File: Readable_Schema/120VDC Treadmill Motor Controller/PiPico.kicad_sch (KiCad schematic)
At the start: 5 parts, among them J3 TB0011-350-08BE, J4 TB0011-350-08BE, J5 TB0011-350-08BE

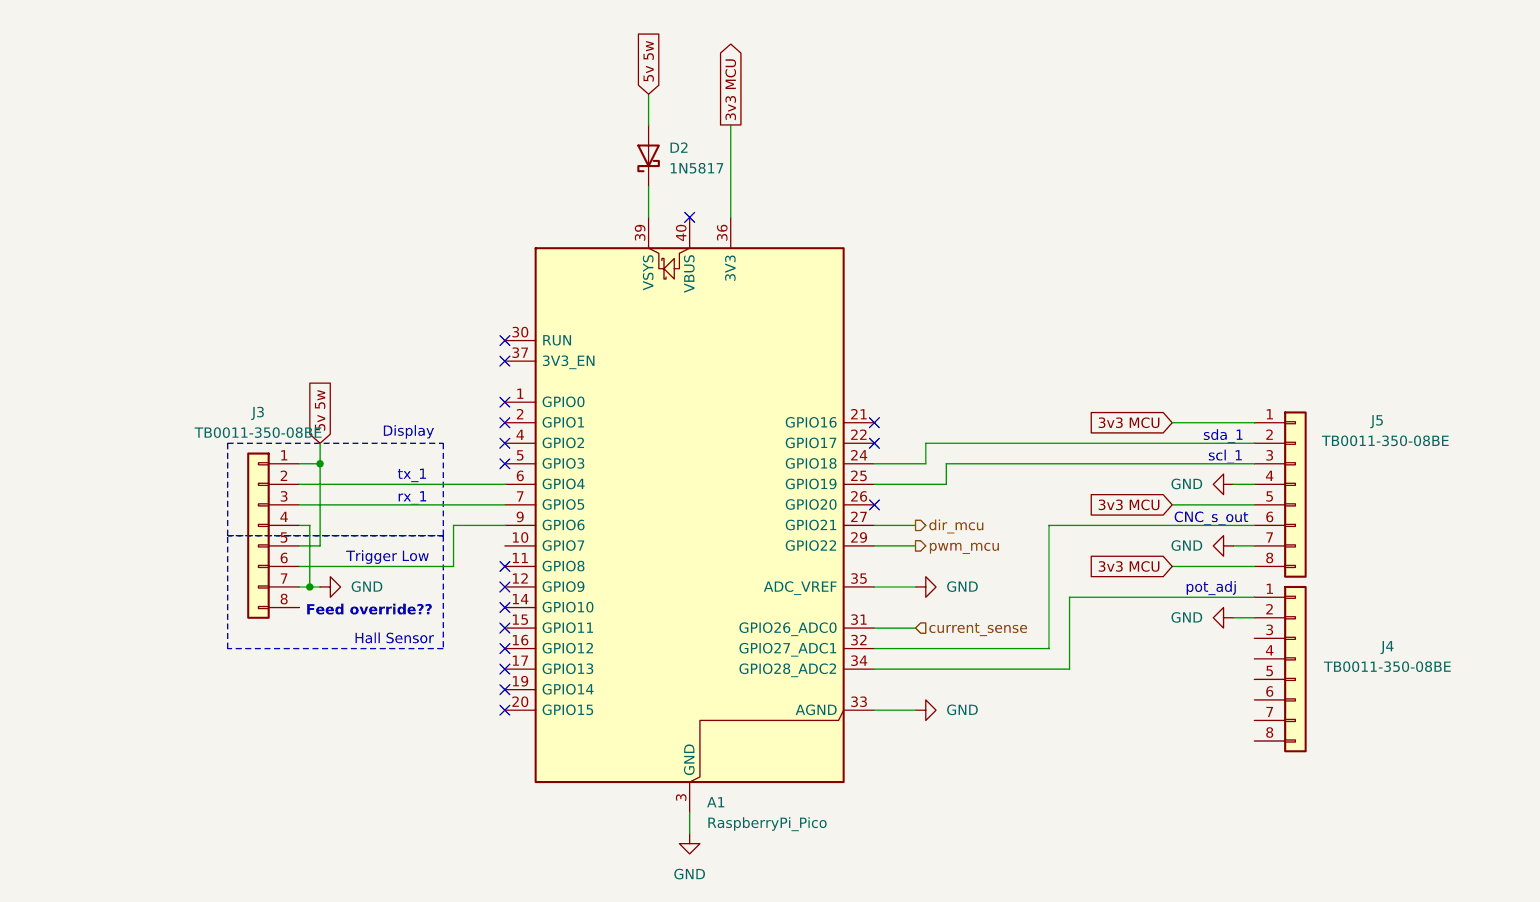
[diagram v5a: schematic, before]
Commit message: started working on the e_stop circuit. Basically just using a relay to shut off all power to the system, including both the mcu and the 170 DC 120HZ.
-Need to finish the E_stop subcircuit
-Still need to start wrapping up the brake resistor subcircuit
-input capacitor sizing
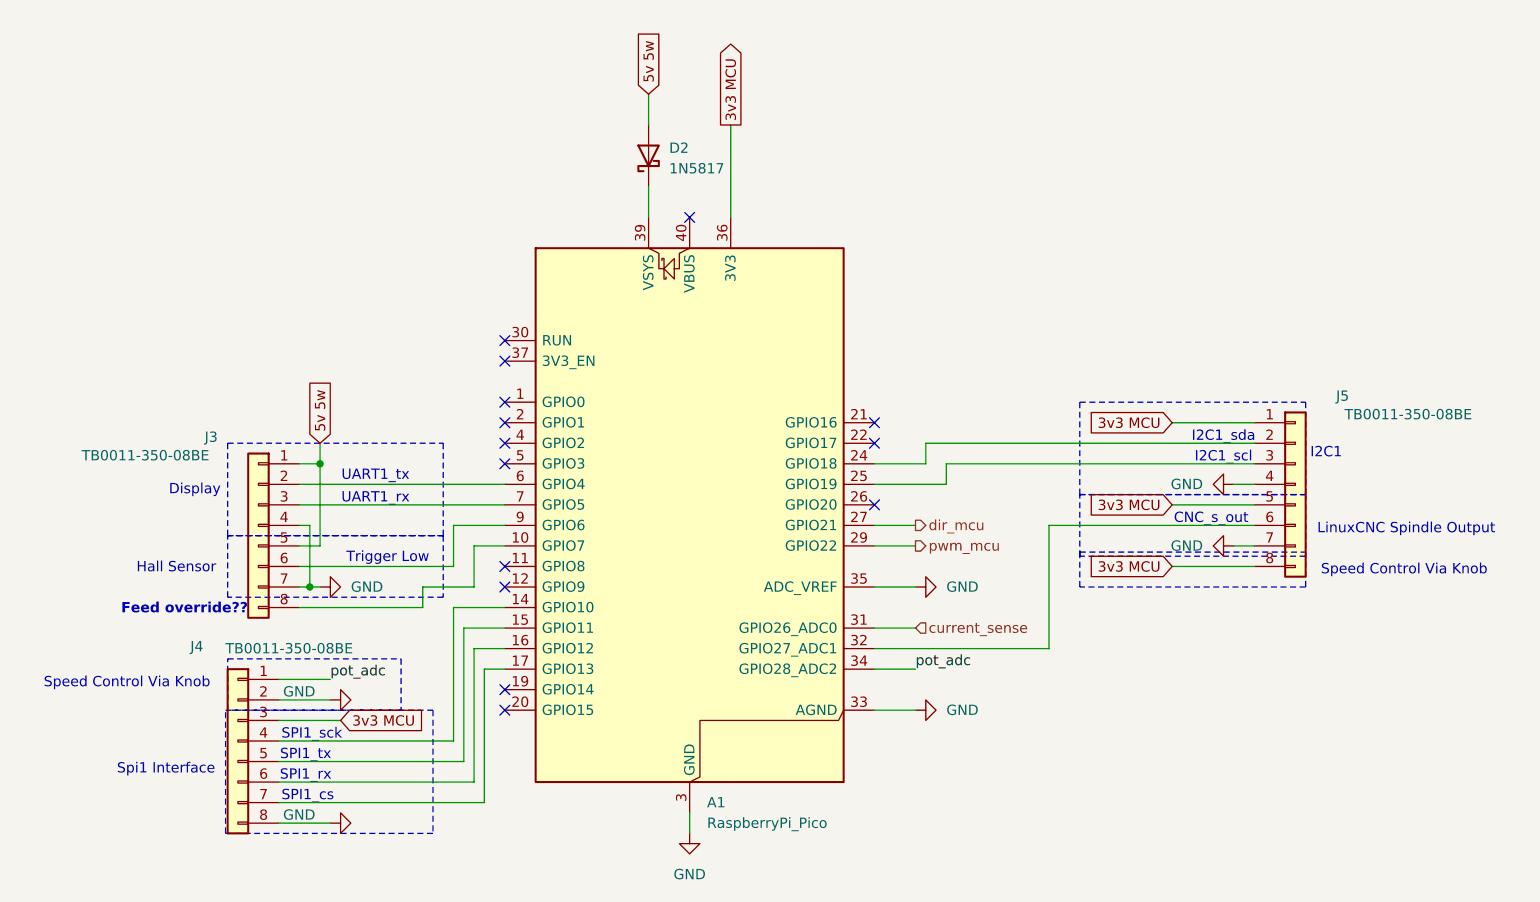
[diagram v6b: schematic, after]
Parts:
- J3, J4, J5: footprint Connector_Wago:Wago_734-138_1x08_P3.50mm_Vertical -> Treadmill_Feet:SAMESKY_TB0011-350-08BE
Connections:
- net 3v3 MCU: now also J4.3 (Pin_3)
- net GND: now also J4.8 (Pin_8)
- net at A1.10 (GPIO7): now also J3.8 (Pin_8)
- net at A1.14 (GPIO10): now also J4.4 (Pin_4)
- net at A1.15 (GPIO11): now also J4.5 (Pin_5)
- net at A1.16 (GPIO12): now also J4.6 (Pin_6)
- net at A1.17 (GPIO13): now also J4.7 (Pin_7)
- net pot_adc: now reaches A1.34 (GPIO28_ADC2), J4.1 (Pin_1)
- no-connect marks 18 -> 14
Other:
- note added: "I2C1"
- note added: "I2C1_scl"
- note added: "I2C1_sda"
- note added: "LinuxCNC Spindle Output"
- note added: "SPI1_cs"
- note added: "SPI1_rx"
- note added: "SPI1_sck"
- note added: "SPI1_tx"
- note added: "Speed Control Via Knob"
- note added: "Spi1 Interface"
- note added: "UART1_rx"
- note added: "UART1_tx"
- note removed: "pot_adj"
- note removed: "rx_1"
- note removed: "scl_1"
- note removed: "sda_1"
- note removed: "tx_1"

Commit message: we have reached the point of starting to roughly place where components should go (have not started messing with traces). -Confirm heatsink size so that we can block that area out on the schema -add some test points similar to what we were testing in ltspice to determine functionality of the device -Review general layout with dad to confirm we r good to start drawing traces
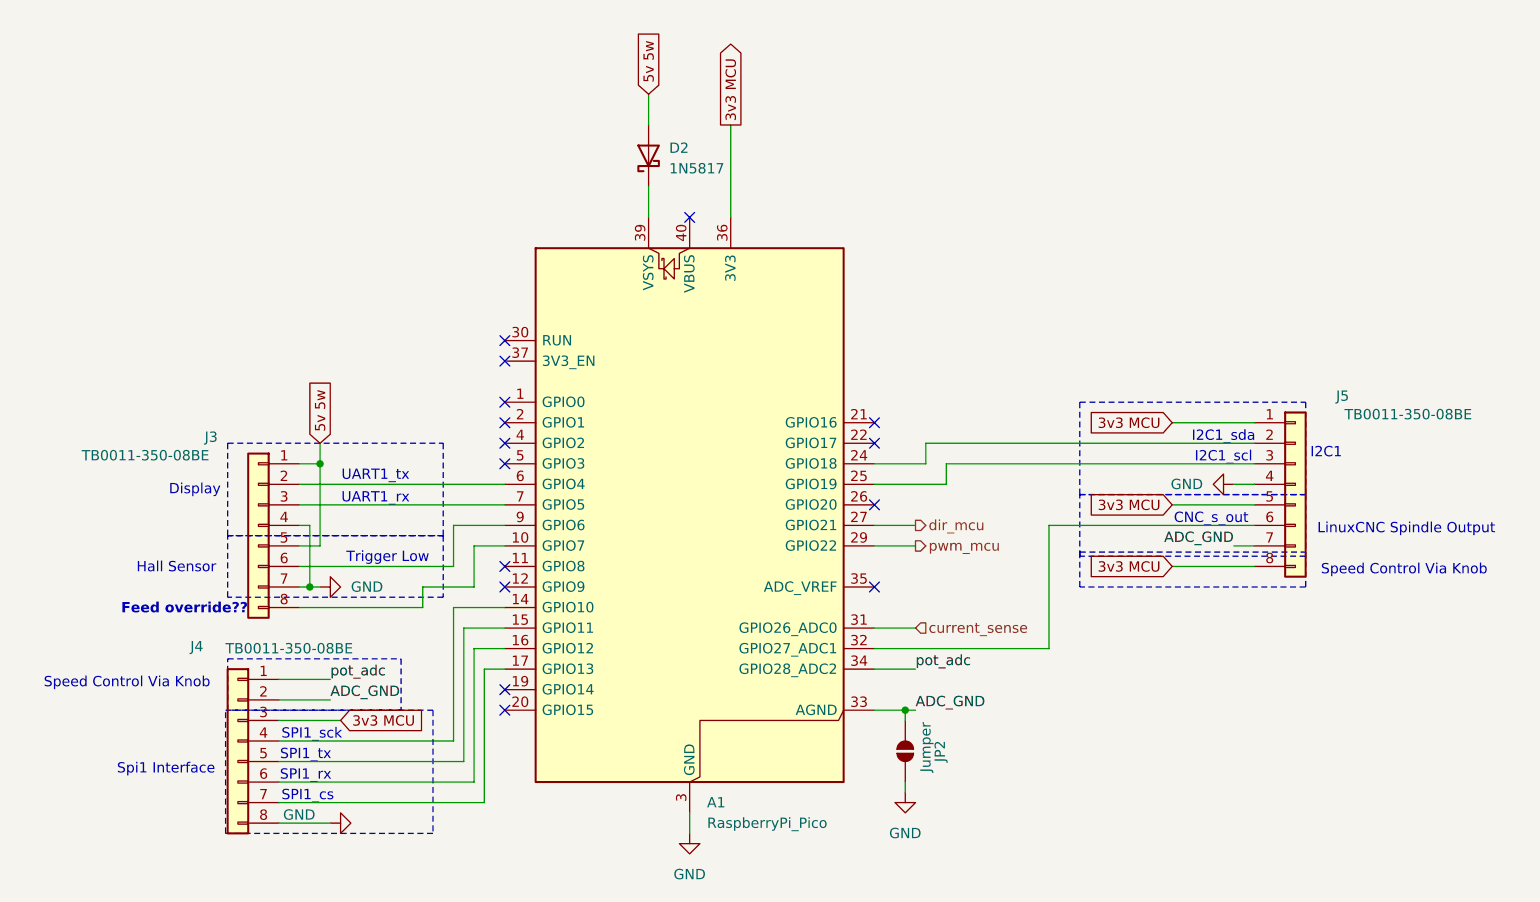
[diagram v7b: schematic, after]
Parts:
- added JP2: Jumper, Jumper:SolderJumper-2_P1.3mm_Open_RoundedPad1.0x1.5mm, symbol Jumper:SolderJumper_2_Open
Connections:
- net GND: now also JP2.1 (A); no longer A1.33 (AGND), A1.35 (ADC_VREF), J4.2 (Pin_2), J5.7 (Pin_7)
- new net ADC_GND: A1.33 (AGND), J4.2 (Pin_2), J5.7 (Pin_7), JP2.2 (B)
- no-connect marks 14 -> 15
